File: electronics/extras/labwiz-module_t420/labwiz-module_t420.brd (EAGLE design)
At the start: 65.8 x 35.2 mm, 47 parts, among them IC1 MCP3424, U1 MCP9800

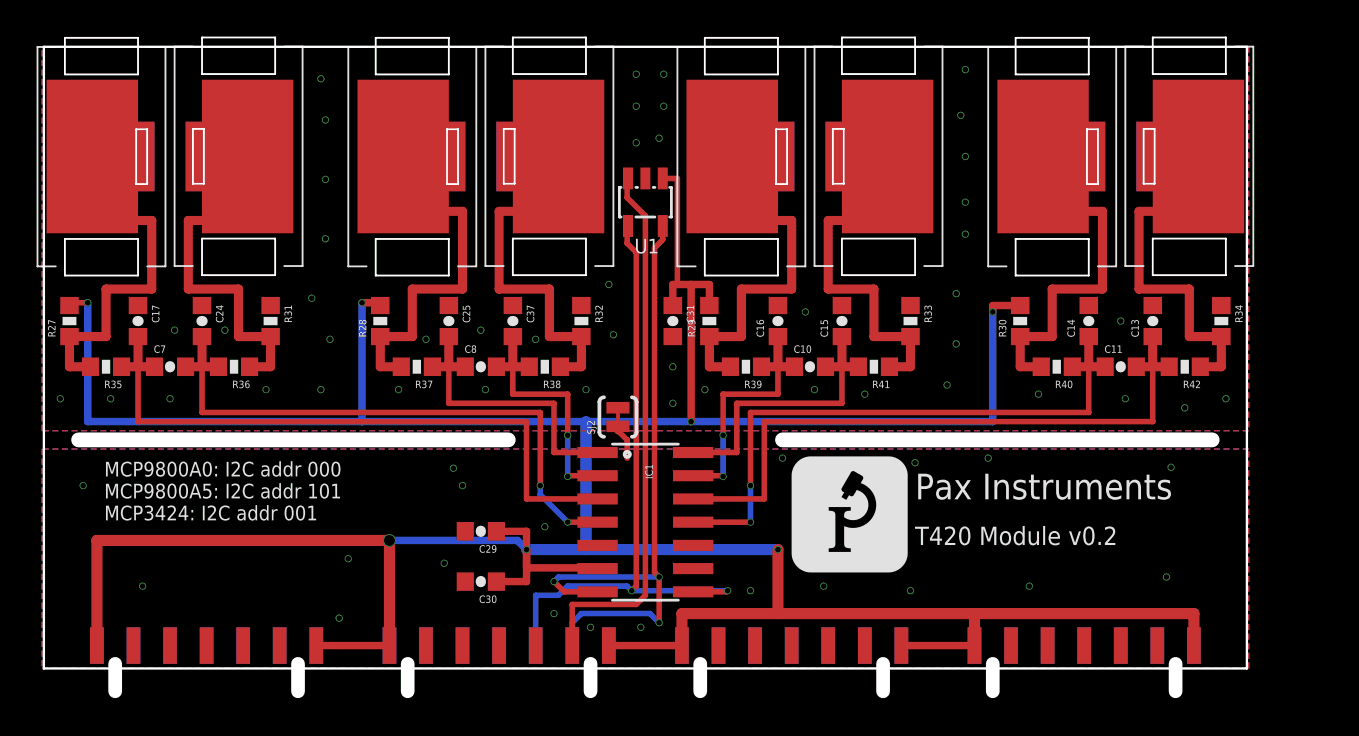
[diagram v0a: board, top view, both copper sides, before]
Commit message: Minor changes after design review. Will begin generating new gerbrs.
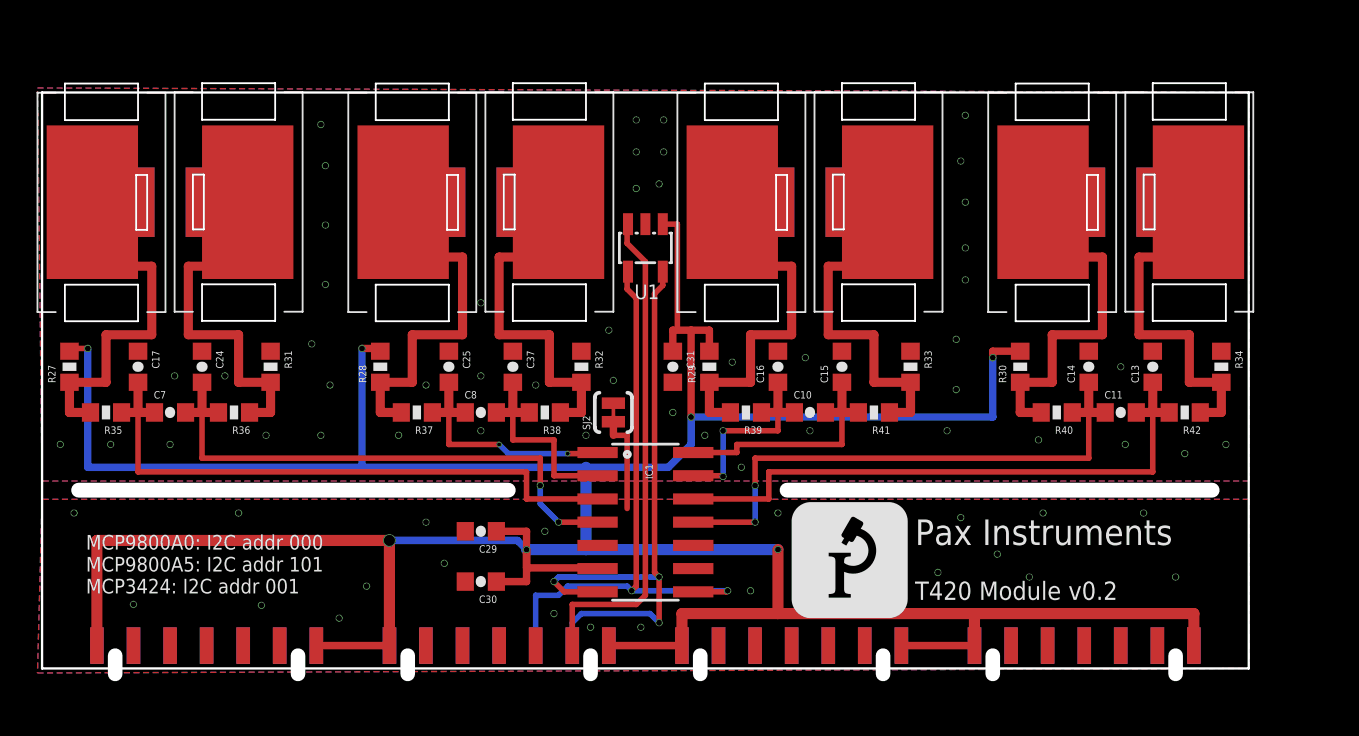
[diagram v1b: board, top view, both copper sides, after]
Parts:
- moved C10 2.50 mm to (42.0, 14.0)
- moved C11 2.50 mm to (59.0, 14.0)
- moved C13 2.50 mm to (60.8, 16.5)
- moved C14 2.50 mm to (57.2, 16.5)
- moved C15 2.50 mm to (43.8, 16.5)
- moved C16 2.50 mm to (40.2, 16.5)
- moved C17 2.50 mm to (5.25, 16.5)
- moved C24 2.50 mm to (8.75, 16.5)
- moved C25 2.50 mm to (22.2, 16.5)
- moved C31 2.50 mm to (34.5, 16.5)
- moved C37 2.50 mm to (25.8, 16.5)
- moved C7 2.50 mm to (7.00, 14.0)
- moved C8 2.50 mm to (24.0, 14.0)
- moved R27 2.50 mm to (1.50, 16.5)
- moved R28 2.50 mm to (18.5, 16.5)
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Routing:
- net 3.3V: track 207.2 -> 201.2 mm
- net GND: track 1.95 -> 5.49 mm, vias 20 -> 21
- net TC2+: track 16.3 -> 13.6 mm, vias 0 -> 2
- net TC2-: track 14.1 -> 11.5 mm, vias 2 -> 0
- net TC4-: track 35.8 -> 33.3 mm
- net TC4+: track 33.6 -> 31.1 mm
- net TC1+: track 35.8 -> 33.3 mm
- net I2C1_SCL: track 35.8 -> 33.3 mm
- net ALERT: track 29.7 -> 27.2 mm
- net TC3+: track 14.1 -> 11.6 mm
- net TC3-: track 16.3 -> 13.8 mm
- net I2C1_SDA: track 36.9 -> 34.4 mm
- net TC1-: track 32.7 -> 30.5 mm
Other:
- board size 65.8 x 35.2 mm -> 66 x 31.5 mm
- board text added: "Height restriction 4.7 mm"

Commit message: Updated full-breakout and T420 modules. Boards ordered.
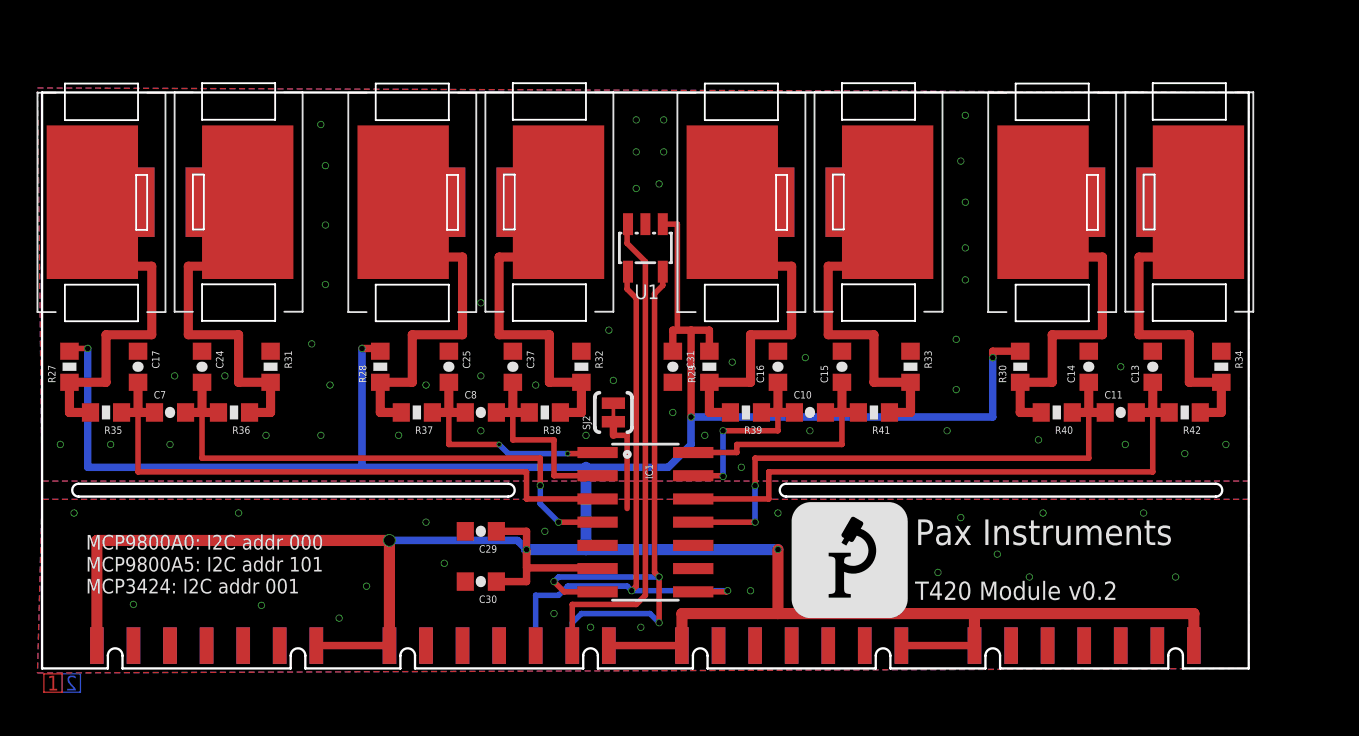
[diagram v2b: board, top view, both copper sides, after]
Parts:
- added U$2: (no value), PaxInstruments-Aesthetics:LAYERS-LABEL-2
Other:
- outline, holes or cut-outs redrawn
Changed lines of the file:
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@@
 <setting verticaltext="up"/>
 </settings>
-<grid distance="0.5" unitdist="mm" unit="mm" style="lines" multiple="1" display="yes" altdistance="0.05" altunitdist="mil" altunit="inch"/>
+<grid distance="0.1" unitdist="mm" unit="mm" style="lines" multiple="1" display="yes" altdistance="0.05" altunitdist="mil" altunit="inch"/>
 <layers>
 <layer number="1" name="Top" color="4" fill="1" visible="yes" active="yes"/>
@@
 <plain>
 <wire x1="0" y1="31.5" x2="0" y2="0" width="0.127" layer="20"/>
-<wire x1="0" y1="0" x2="66" y2="0" width="0.127" layer="20"/>
+<wire x1="0" y1="0" x2="3.6" y2="0" width="0.127" layer="20"/>
+<wire x1="4.4" y1="0" x2="13.6" y2="0" width="0.127" layer="20"/>
+<wire x1="14.4" y1="0" x2="19.6" y2="0" width="0.127" layer="20"/>
+<wire x1="20.4" y1="0" x2="29.6" y2="0" width="0.127" layer="20"/>
+<wire x1="30.4" y1="0" x2="35.6" y2="0" width="0.127" layer="20"/>
+<wire x1="36.4" y1="0" x2="45.6" y2="0" width="0.127" layer="20"/>
+<wire x1="46.4" y1="0" x2="51.6" y2="0" width="0.127" layer="20"/>
+<wire x1="52.4" y1="0" x2="61.6" y2="0" width="0.127" layer="20"/>
+<wire x1="62.4" y1="0" x2="66" y2="0" width="0.127" layer="20"/>
 <wire x1="66" y1="0" x2="66" y2="31.5" width="0.127" layer="20"/>
 <wire x1="66" y1="31.5" x2="0" y2="31.5" width="0.127" layer="20"/>
@@
 <dimension x1="0" y1="31.5" x2="66" y2="31.5" x3="33" y3="36.25" textsize="1.778" layer="47" dtype="horizontal"/>
 <dimension x1="-7" y1="0" x2="-8" y2="100" x3="-11.5" y3="50" textsize="1.778" layer="47" dtype="vertical"/>
-<wire x1="25.5" y1="9.75" x2="2" y2="9.75" width="0.8128" layer="46"/>
-<wire x1="64" y1="9.75" x2="40.75" y2="9.75" width="0.8128" layer="46"/>
 <text x="47.75" y="6.75" size="1.4" layer="21" font="vector">Pax Instruments</text>
 <text x="47.75" y="3.75" size="1" layer="21" font="vector">T420 Module v0.2</text>
@@
 MCP3424: I2C addr 001</text>
 <rectangle x1="31.5" y1="26.5" x2="34.5" y2="27.5" layer="39"/>
-<text x="-19" y="15.5" size="1.778" layer="43">Height restriction
+<text x="2.8" y="-5" size="1.778" layer="43">Height restriction
 4.7 mm</text>
-<wire x1="-9" y1="16.5" x2="-0.5" y2="16.5" width="0.3048" layer="43"/>
-<wire x1="-0.5" y1="16.5" x2="-1.5" y2="17" width="0.3048" layer="43"/>
-<wire x1="-1.5" y1="17" x2="-1.5" y2="16" width="0.3048" layer="43"/>
-<wire x1="-1.5" y1="16" x2="-0.5" y2="16.5" width="0.3048" layer="43"/>
 <rectangle x1="0" y1="0" x2="66" y2="34.5" layer="43"/>
+<wire x1="3.6" y1="0" x2="3.6" y2="0.7" width="0.127" layer="20"/>
+<wire x1="4.4" y1="0" x2="4.4" y2="0.7" width="0.127" layer="20"/>
+<wire x1="3.6" y1="0.7" x2="4.4" y2="0.7" width="0.127" layer="20" curve="-180"/>
+<wire x1="13.6" y1="0.7" x2="14.4" y2="0.7" width="0.127" layer="20" curve="-180"/>
+<wire x1="19.6" y1="0.7" x2="20.4" y2="0.7" width="0.127" layer="20" curve="-180"/>
+<wire x1="29.6" y1="0.7" x2="30.4" y2="0.7" width="0.127" layer="20" curve="-180"/>
+<wire x1="35.6" y1="0.7" x2="36.4" y2="0.7" width="0.127" layer="20" curve="-180"/>
+<wire x1="45.6" y1="0.7" x2="46.4" y2="0.7" width="0.127" layer="20" curve="-180"/>
+<wire x1="51.6" y1="0.7" x2="52.4" y2="0.7" width="0.127" layer="20" curve="-180"/>
+<wire x1="61.6" y1="0.7" x2="62.4" y2="0.7" width="0.127" layer="20" curve="-180"/>
+<wire x1="13.6" y1="0" x2="13.6" y2="0.7" width="0.127" layer="20"/>
+<wire x1="14.4" y1="0" x2="14.4" y2="0.7" width="0.127" layer="20"/>
+<wire x1="19.6" y1="0" x2="19.6" y2="0.7" width="0.127" layer="20"/>
+<wire x1="20.4" y1="0" x2="20.4" y2="0.7" width="0.127" layer="20"/>
+<wire x1="29.6" y1="0" x2="29.6" y2="0.7" width="0.127" layer="20"/>
+<wire x1="30.4" y1="0" x2="30.4" y2="0.7" width="0.127" layer="20"/>
+<wire x1="35.6" y1="0" x2="35.6" y2="0.7" width="0.127" layer="20"/>
+<wire x1="36.4" y1="0" x2="36.4" y2="0.7" width="0.127" layer="20"/>
+<wire x1="45.6" y1="0" x2="45.6" y2="0.7" width="0.127" layer="20"/>
+<wire x1="46.4" y1="0" x2="46.4" y2="0.7" width="0.127" layer="20"/>
+<wire x1="51.6" y1="0" x2="51.6" y2="0.7" width="0.127" layer="20"/>
+<wire x1="52.4" y1="0" x2="52.4" y2="0.7" width="0.127" layer="20"/>
+<wire x1="61.6" y1="0" x2="61.6" y2="0.7" width="0.127" layer="20"/>
+<wire x1="62.4" y1="0" x2="62.4" y2="0.7" width="0.127" layer="20"/>
+<wire x1="2" y1="9.4" x2="2" y2="10.1" width="0.127" layer="20" curve="-180"/>
+<wire x1="2" y1="9.4" x2="25.5" y2="9.4" width="0.127" layer="20"/>
+<wire x1="25.5" y1="10.1" x2="25.5" y2="9.4" width="0.127" layer="20" curve="-180"/>
+<wire x1="2" y1="10.1" x2="25.5" y2="10.1" width="0.127" layer="20"/>
+<wire x1="40.7" y1="9.4" x2="40.7" y2="10.1" width="0.127" layer="20" curve="-180"/>
+<wire x1="40.7" y1="9.4" x2="64.2" y2="9.4" width="0.127" layer="20"/>
+<wire x1="64.2" y1="10.1" x2="64.2" y2="9.4" width="0.127" layer="20" curve="-180"/>
+<wire x1="40.7" y1="10.1" x2="64.2" y2="10.1" width="0.127" layer="20"/>
 </plain>
 <attributes>
@@
 </element>
 <element name="U$1" library="PaxInstruments-Aesthetics" package="PAX-LOGO-0.25IN" value="" x="41" y="2.75"/>
+<element name="U$2" library="PaxInstruments-Aesthetics" package="LAYERS-LABEL-2" value="" x="0.1" y="-1.3"/>
 </elements>
 <signals>

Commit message: Updated .gitignore. Comitting unknown schematic updates.
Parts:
- moved MODULE8 4.25 mm to (67.2, 1.00)
- moved MODULE7 2.75 mm to (49.8, 1.00)
- moved C11 2.25 mm to (61.2, 14.0)
- moved C13 2.25 mm to (63.0, 16.5)
- moved C14 2.25 mm to (59.5, 16.5)
- moved C25 2.25 mm to (24.5, 16.5)
- moved C37 2.25 mm to (28.0, 16.5)
- moved C8 2.25 mm to (26.2, 14.0)
- moved R28 2.25 mm to (20.8, 16.5)
- moved R30 2.25 mm to (55.8, 16.5)
- moved R32 2.25 mm to (31.8, 16.5)
- moved R34 2.25 mm to (66.8, 16.5)
- moved R37 2.25 mm to (22.8, 14.0)
- moved R38 2.25 mm to (29.8, 14.0)
- moved R40 2.25 mm to (57.8, 14.0)
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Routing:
- net 3.3V: track 201.2 -> 210.4 mm
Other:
- board size 66 x 31.5 mm -> 69.9 x 31.5 mm
- board text added: "T420 Module v0.3"
- board text removed: "T420 Module v0.2"
